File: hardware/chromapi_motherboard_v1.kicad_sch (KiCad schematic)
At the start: 9 parts

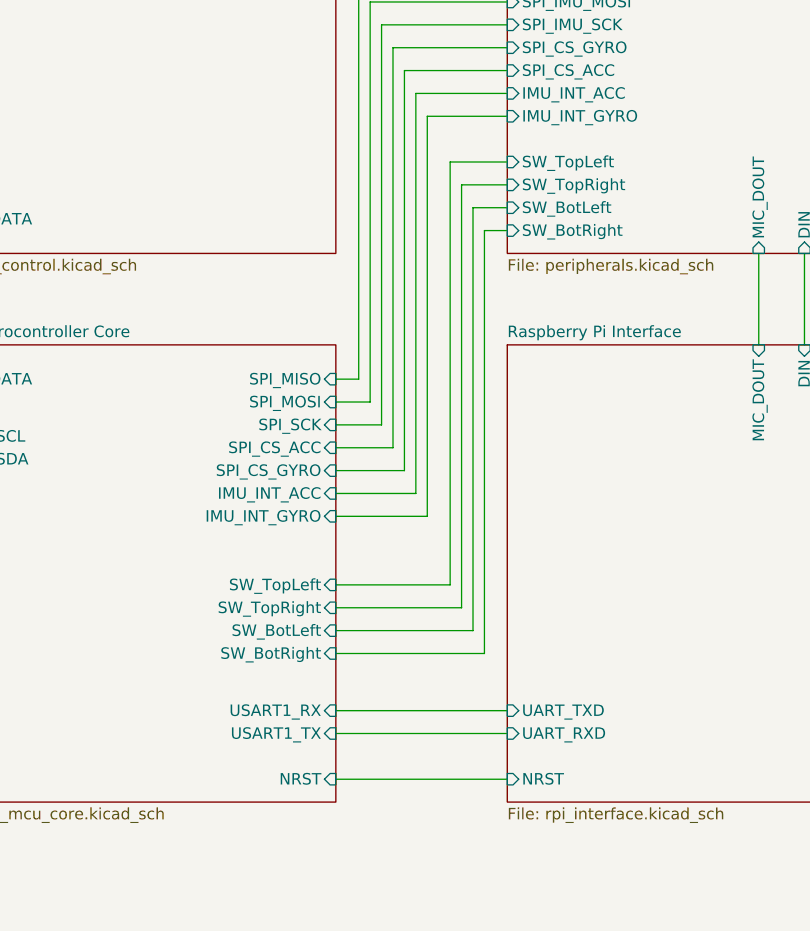
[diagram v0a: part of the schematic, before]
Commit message: schematic update
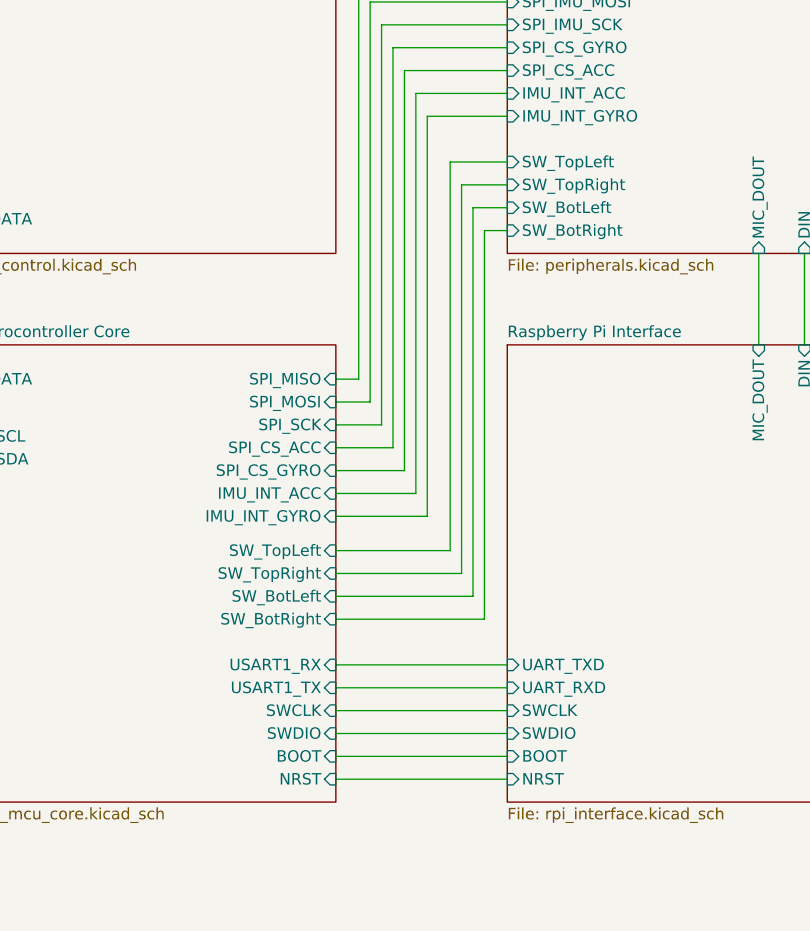
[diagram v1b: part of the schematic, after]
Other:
- sheet Raspberry Pi Interface ports: added BOOT, SWCLK, SWDIO; removed none
- sheet STM32 Microcontroller Core ports: added BOOT, SWCLK, SWDIO; removed none
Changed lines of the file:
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@@
 	(wire
 		(pts
+			(xy 212.09 146.05) (xy 231.14 146.05)
+		)
+		(stroke
+			(width 0)
+			(type default)
+		)
+	)
+	(wire
+		(pts
 			(xy 212.09 121.92) (xy 222.25 121.92)
 		)
@@
 	(wire
 		(pts
-			(xy 227.33 87.63) (xy 227.33 134.62)
+			(xy 227.33 87.63) (xy 227.33 130.81)
 		)
 		(stroke
@@
 	(wire
 		(pts
-			(xy 224.79 129.54) (xy 212.09 129.54)
+			(xy 224.79 125.73) (xy 212.09 125.73)
 		)
 		(stroke
@@
 	(wire
 		(pts
-			(xy 227.33 134.62) (xy 212.09 134.62)
+			(xy 227.33 130.81) (xy 212.09 130.81)
 		)
 		(stroke
@@
 	(wire
 		(pts
-			(xy 212.09 143.51) (xy 231.14 143.51)
+			(xy 212.09 138.43) (xy 231.14 138.43)
 		)
 		(stroke
@@
 	(wire
 		(pts
-			(xy 226.06 132.08) (xy 212.09 132.08)
+			(xy 226.06 128.27) (xy 212.09 128.27)
 		)
 		(stroke
@@
 	(wire
 		(pts
+			(xy 212.09 143.51) (xy 231.14 143.51)
+		)
+		(stroke
+			(width 0)
+			(type default)
+		)
+	)
+	(wire
+		(pts
 			(xy 156.21 113.03) (xy 165.1 113.03)
 		)
@@
 	(wire
 		(pts
-			(xy 224.79 82.55) (xy 224.79 129.54)
+			(xy 224.79 82.55) (xy 224.79 125.73)
 		)
 		(stroke
@@
 	(wire
 		(pts
-			(xy 228.6 90.17) (xy 228.6 137.16)
+			(xy 228.6 90.17) (xy 228.6 133.35)
 		)
 		(stroke
@@
 	(wire
 		(pts
-			(xy 212.09 146.05) (xy 231.14 146.05)
+			(xy 212.09 140.97) (xy 231.14 140.97)
 		)
 		(stroke
@@
 	(wire
 		(pts
-			(xy 228.6 137.16) (xy 212.09 137.16)
+			(xy 212.09 148.59) (xy 231.14 148.59)
+		)
+		(stroke
+			(width 0)
+			(type default)
+		)
+	)
+	(wire
+		(pts
+			(xy 228.6 133.35) (xy 212.09 133.35)
 		)
 		(stroke
@@
 	(wire
 		(pts
-			(xy 226.06 85.09) (xy 226.06 132.08)
+			(xy 226.06 85.09) (xy 226.06 128.27)
 		)
 		(stroke
@@
 		)
 		(pin "USART1_RX" input
-			(at 212.09 143.51 0)
+			(at 212.09 138.43 0)
 			(effects
 				(font
@@
 		)
 		(pin "USART1_TX" input
-			(at 212.09 146.05 0)
+			(at 212.09 140.97 0)
 			(effects
 				(font
@@
 		)
 		(pin "SW_BotRight" input
-			(at 212.09 137.16 0)
+			(at 212.09 133.35 0)
 			(effects
 				(font
@@
 		)
 		(pin "SW_TopRight" input
-			(at 212.09 132.08 0)
+			(at 212.09 128.27 0)
 			(effects
 				(font
@@
 		)
 		(pin "SW_TopLeft" input
-			(at 212.09 129.54 0)
+			(at 212.09 125.73 0)
 			(effects
 				(font
@@
 		)
 		(pin "SW_BotLeft" input
-			(at 212.09 134.62 0)
+			(at 212.09 130.81 0)
+			(effects
+				(font
+					(size 1.27 1.27)
+				)
+				(justify right)
+			)
+		)
+		(pin "BOOT" input
+			(at 212.09 148.59 0)
+			(effects
+				(font
+					(size 1.27 1.27)
+				)
+				(justify right)
+			)
+		)
+		(pin "SWDIO" input
+			(at 212.09 146.05 0)
+			(effects
+				(font
+					(size 1.27 1.27)
+				)
+				(justify right)
+			)
+		)
+		(pin "SWCLK" input
+			(at 212.09 143.51 0)
 			(effects
 				(font
@@
 		)
 		(pin "UART_TXD" input
-			(at 231.14 143.51 180)
+			(at 231.14 138.43 180)
 			(effects
 				(font
@@
 		)
 		(pin "UART_RXD" input
+			(at 231.14 140.97 180)
+			(effects
+				(font
+					(size 1.27 1.27)
+				)
+				(justify left)
+			)
+		)
+		(pin "BOOT" input
+			(at 231.14 148.59 180)
+			(effects
+				(font
+					(size 1.27 1.27)
+				)
+				(justify left)
+			)
+		)
+		(pin "SWCLK" input
+			(at 231.14 143.51 180)
+			(effects
+				(font
+					(size 1.27 1.27)
+				)
+				(justify left)
+			)
+		)
+		(pin "SWDIO" input
 			(at 231.14 146.05 180)
 			(effects

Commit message: replacing components
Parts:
- removed TP1: TP_GND, TestPoint:TestPoint_Pad_D1.5mm, symbol Connector:TestPoint
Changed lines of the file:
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@@
 	(wire
 		(pts
-			(xy 140.97 187.96) (xy 143.51 187.96)
-		)
-		(stroke
-			(width 0)
-			(type default)
-		)
-	)
-	(wire
-		(pts
 			(xy 226.06 128.27) (xy 212.09 128.27)
 		)
@@
 					(unit 1)
 				)
-			)
-		)
-	)
-	(symbol
-		(lib_id "Connector:TestPoint")
-		(at 140.97 187.96 90)
-		(unit 1)
-		(body_style 1)
-		(exclude_from_sim no)
-		(in_bom no)
-		(on_board yes)
-		(in_pos_files yes)
-		(dnp no)
-		(fields_autoplaced yes)
-		(property "Reference" "TP1"
-			(at 137.668 182.88 90)
-			(show_name no)
-			(do_not_autoplace no)
-			(effects
-				(font
-					(size 1.27 1.27)
-				)
-			)
-		)
-		(property "Value" "TP_GND"
-			(at 137.668 185.42 90)
-			(show_name no)
-			(do_not_autoplace no)
-			(effects
-				(font
-					(size 1.27 1.27)
-				)
-			)
-		)
-		(property "Footprint" "TestPoint:TestPoint_Pad_D1.5mm"
-			(at 140.97 182.88 0)
-			(hide yes)
-			(show_name no)
-			(do_not_autoplace no)
-			(effects
-				(font
-					(size 1.27 1.27)
-				)
-			)
-		)
-		(property "Datasheet" ""
-			(at 140.97 182.88 0)
-			(hide yes)
-			(show_name no)
-			(do_not_autoplace no)
-			(effects
-				(font
-					(size 1.27 1.27)
-				)
-			)
-		)
-		(property "Description" "test point"
-			(at 140.97 187.96 0)
-			(hide yes)
-			(show_name no)
-			(do_not_autoplace no)
-			(effects
-				(font
-					(size 1.27 1.27)
-				)
-			)
-		)
-		(property "Author" ""
-			(at 140.97 187.96 90)
-			(hide yes)
-			(show_name no)
-			(do_not_autoplace no)
-			(effects
-				(font
-					(size 1.27 1.27)
-				)
-			)
-		)
-		(property "License" ""
-			(at 140.97 187.96 90)
-			(hide yes)
-			(show_name no)
-			(do_not_autoplace no)
-			(effects
-				(font
-					(size 1.27 1.27)
-				)
-			)
-		)
-		(property "Manufacturer" ""
-			(at 140.97 187.96 90)
-			(hide yes)
-			(show_name no)
-			(do_not_autoplace no)
-			(effects
-				(font
-					(size 1.27 1.27)
-				)
-			)
-		)
-		(property "MP" ""
-			(at 140.97 187.96 90)
-			(hide yes)
-			(show_name no)
-			(do_not_autoplace no)
-			(effects
-				(font
-					(size 1.27 1.27)
-				)
-			)
-		)
-		(property "MANUFACTURER" ""
-			(at 140.97 187.96 90)
-			(hide yes)
-			(show_name no)
-			(do_not_autoplace no)
-			(effects
-				(font
-					(size 1.27 1.27)
-				)
-			)
-		)
-		(property "MAXIMUM_PACKAGE_HEIGHT" ""
-			(at 140.97 187.96 90)
-			(hide yes)
-			(show_name no)
-			(do_not_autoplace no)
-			(effects
-				(font
-					(size 1.27 1.27)
-				)
-			)
-		)
-		(property "PARTREV" ""
-			(at 140.97 187.96 90)
-			(hide yes)
-			(show_name no)
-			(do_not_autoplace no)
-			(effects
-				(font
-					(size 1.27 1.27)
-				)
-			)
-		)
-		(pin "1"
-		)
-		(instances
-			(project "chromapi_motherboard_v1"
-				(path "/d1a31f26-03e0-43e1-89c1-031fe31befc5"
-					(reference "TP1")
-					(unit 1)
-				)

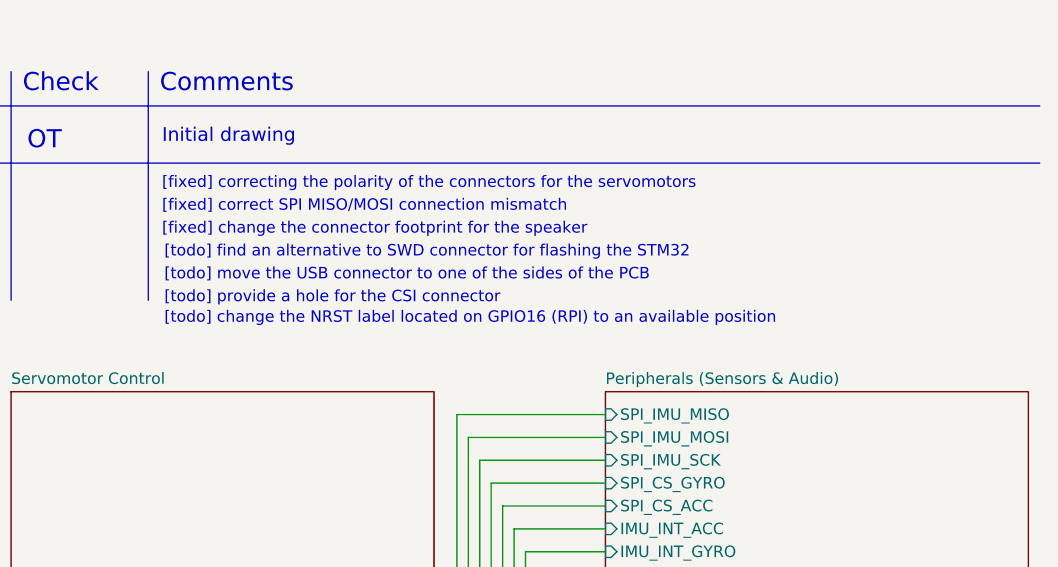
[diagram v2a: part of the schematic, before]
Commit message: update schematic
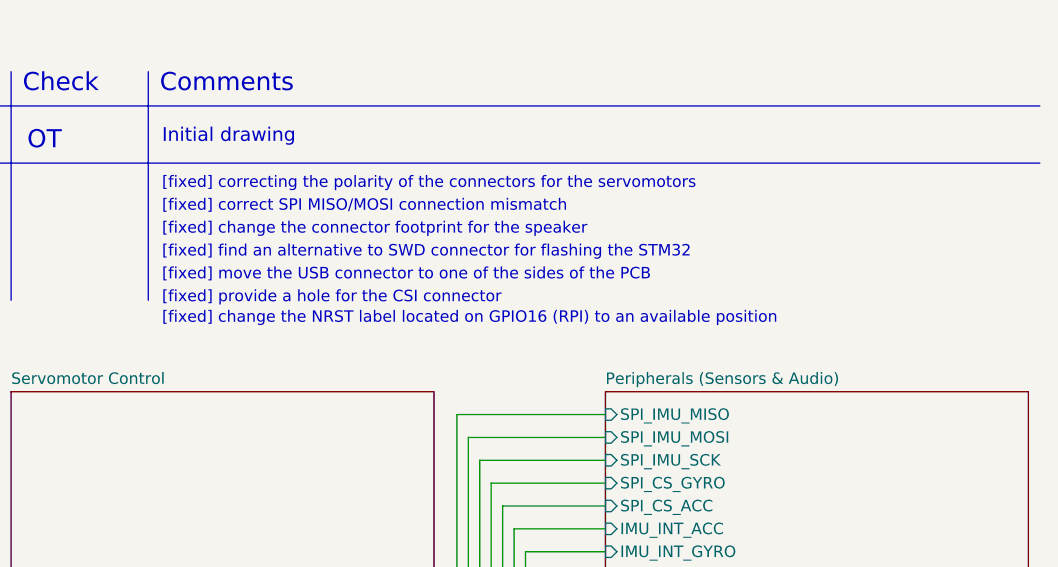
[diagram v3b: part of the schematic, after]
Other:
- note added: "[fixed] change the NRST label located on GPIO16 (RPI) to an available position"
- note added: "[fixed] find an alternative to SWD connector for flashing the STM32"
- note added: "[fixed] move the USB connector to one of the sides of the PCB"
- note added: "[fixed] provide a hole for the CSI connector"
- note removed: "[todo] change the NRST label located on GPIO16 (RPI) to an available position"
- note removed: "[todo] find an alternative to SWD connector for flashing the STM32"
- note removed: "[todo] move the USB connector to one of the sides of the PCB"
- note removed: "[todo] provide a hole for the CSI connector"
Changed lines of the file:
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@@
 		)
 	)
-	(text "[todo] change the NRST label located on GPIO16 (RPI) to an available position"
+	(text "[fixed] change the NRST label located on GPIO16 (RPI) to an available position"
 		(exclude_from_sim no)
-		(at 182.118 52.324 0)
+		(at 181.864 52.324 0)
 		(effects
 			(font
@@
 		)
 	)
-	(text "[todo] provide a hole for the CSI connector "
+	(text "[fixed] provide a hole for the CSI connector "
 		(exclude_from_sim no)
-		(at 182.118 50.038 0)
+		(at 181.864 50.038 0)
 		(effects
 			(font
@@
 		)
 	)
-	(text "[todo] move the USB connector to one of the sides of the PCB"
+	(text "[fixed] move the USB connector to one of the sides of the PCB"
 		(exclude_from_sim no)
-		(at 182.118 47.498 0)
+		(at 181.864 47.498 0)
 		(effects
 			(font
@@
 		)
 	)
-	(text "[todo] find an alternative to SWD connector for flashing the STM32"
+	(text "[fixed] find an alternative to SWD connector for flashing the STM32"
 		(exclude_from_sim no)
-		(at 182.118 44.958 0)
+		(at 181.864 44.958 0)
 		(effects
 			(font
@@
 			)
 		)
-		(property "Manufacturer" ""
+		(property "MANUFACTURER" ""
 			(at 156.21 182.88 90)
 			(hide yes)
@@
 			)
 		)
-		(property "Manufacturer" ""
+		(property "MANUFACTURER" ""
 			(at 125.73 181.61 0)
 			(hide yes)
@@
 			)
 		)
-		(property "Manufacturer" ""
+		(property "MANUFACTURER" ""
 			(at 149.86 182.88 90)
 			(hide yes)
@@
 			)
 		)
-		(property "Manufacturer" ""
+		(property "MANUFACTURER" ""
 			(at 120.65 189.23 0)
 			(hide yes)
@@
 			)
 		)
-		(property "Manufacturer" ""
+		(property "MANUFACTURER" ""
 			(at 115.57 181.61 0)
 			(hide yes)
@@
 			)
 		)
-		(property "Manufacturer" ""
+		(property "MANUFACTURER" ""
 			(at 143.51 182.88 90)
 			(hide yes)
@@
 			)
 		)
-		(property "Manufacturer" ""
+		(property "MANUFACTURER" ""
 			(at 134.62 168.91 0)
 			(hide yes)
@@
 			)
 		)
-		(property "Manufacturer" ""
+		(property "MANUFACTURER" ""
 			(at 162.56 182.88 90)
 			(hide yes)
